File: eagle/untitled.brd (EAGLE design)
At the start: 50 x 50 mm, 58 parts, among them J1 JTAG, Q1 16MHz, U1 MMA3202KEG

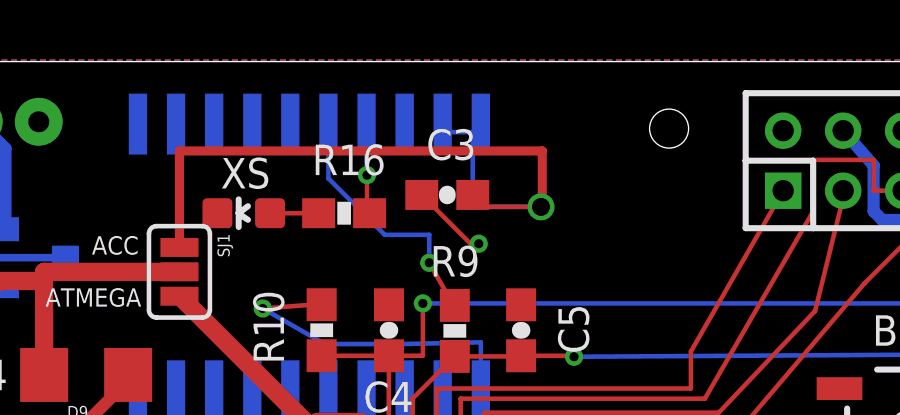
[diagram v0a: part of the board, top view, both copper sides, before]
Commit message: Add self test pad for accelerometer.
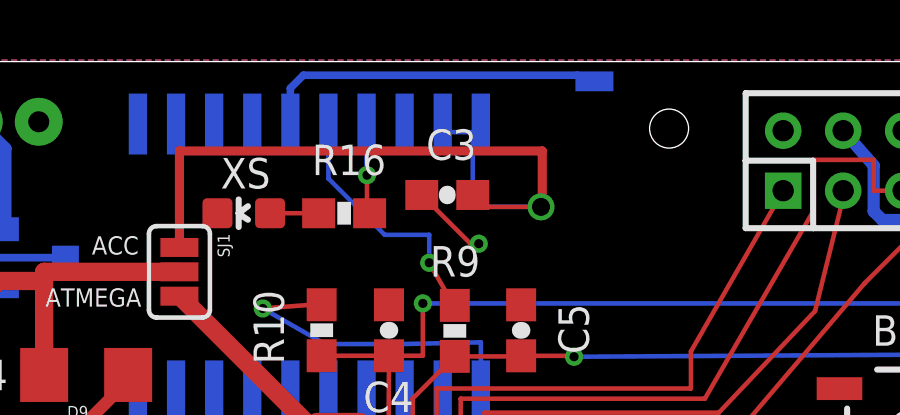
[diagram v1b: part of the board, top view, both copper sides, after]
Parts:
- added TP1: TESTPAD, gipi:TP_SEMICIRCULAR
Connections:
- new net N$28: TP1.P$2, U1.P$5
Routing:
- net N$28: track 0.00 -> 11.6 mm
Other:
- board text added: "S-TEST"
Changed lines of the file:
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@@
 <setting verticaltext="up"/>
 </settings>
-<grid distance="100" unitdist="mil" unit="mil" style="lines" multiple="1" display="yes" altdistance="10" altunitdist="mil" altunit="mil"/>
+<grid distance="100" unitdist="mil" unit="mil" style="lines" multiple="1" display="yes" altdistance="1" altunitdist="mil" altunit="mil"/>
 <layers>
 <layer number="1" name="Top" color="4" fill="1" visible="yes" active="yes"/>
@@
 <hole x="30.48" y="33.02" drill="1.3"/>
 <hole x="35.56" y="76.2" drill="1.3"/>
+<text x="34.3662" y="76.454" size="0.6096" layer="22" font="vector" ratio="16" rot="SMR0">S-TEST</text>
 </plain>
 <attributes>
@@
 <attribute name="VALUE" x="11.26345" y="69.99168125" size="1.27" layer="28" rot="MR90"/>
 </element>
+<element name="TP1" library="gipi" package="TP_SEMICIRCULAR" value="TESTPAD" x="33.0708" y="77.7748" rot="MR0"/>
 </elements>
 <signals>
@@
 <wire x1="13.43845" y1="75.5376375" x2="13.43845" y2="72.84668125" width="0.4064" layer="16"/>
 </signal>
+<signal name="N$28">
+<contactref element="U1" pad="P$5"/>
+<wire x1="22.935309375" y1="76.349809375" x2="22.935309375" y2="77.545309375" width="0.254" layer="16"/>
+<wire x1="22.935309375" y1="77.545309375" x2="23.368" y2="77.978" width="0.254" layer="16"/>
+<wire x1="23.368" y1="77.978" x2="32.512" y2="77.978" width="0.254" layer="16"/>
+<contactref element="TP1" pad="P$2"/>
+<wire x1="32.512" y1="77.978" x2="32.639" y2="77.851" width="0.254" layer="16"/>
+<wire x1="32.639" y1="77.851" x2="33.0708" y2="77.7748" width="0.254" layer="16"/>
+</signal>
 </signals>

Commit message: 2nd version in production.
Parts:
- BOOST: value V_REG_TPS61040SMD -> TPS61040
- D13: value DIODE -> MBRA140; device gipi:1206 -> SparkFun-DiscreteSemi:SMA-DIODE
- L1: value (none) -> 3.3uH; device SparkFun-Passives:0603 -> SparkFun-Passives:1210
- N-FET: value P-CHANNEL-MOSFET -> N-CHANNEL-MOSFET-BSS138
- RA: value 1k -> 3.09k
- moved L1 0.80 mm to (8.53, 71.9)
- renumbered R17 to RA, R18 to RB
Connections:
- net N$39: now also D13.A; no longer D13.P$1
- net VBATT: now also D13.C; no longer D13.P$2
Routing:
- net N$38: track 10.2 -> 11.0 mm
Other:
- board text added: "V2"

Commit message: Fix mess with ground.
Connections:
- removed net GN: C4.1, C5.1, C6.2, D1.C, D2.C, D3.C, D4.C, D5.C, D6.C, D7.C, D8.C, D9.C, J1.10, J1.2, JP1.12, JP5.6, S1.1, S1.2, S2.3, XS.C
- removed net GND-ISO: BOOST.2, C1.1, C2.1, C3.1, C7.1, C9.1, JP2.GND, JP6.2, N-FET.1, RB.1, U$1.15, U$1.23, U$1.35, U$1.43, U$1.5, U1.P$20, U1.P$8
- new net GND: BOOST.2, C1.1, C2.1, C3.1, C4.1, C5.1, C6.2, C7.1, C9.1, D1.C, D2.C, D3.C, D4.C, D5.C, D6.C, D7.C, D8.C, D9.C, J1.10, J1.2, JP1.12, JP2.GND, JP5.6, JP6.2, N-FET.1, RB.1, S1.1, S1.2, S2.3, U$1.15, U$1.23, U$1.35, U$1.43, U$1.5, U1.P$20, U1.P$8, XS.C
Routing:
- net GND-ISO: track 27.2 -> 0.00 mm, vias 6 -> 0
- net GN: track 5.72 -> 0.01 mm
- added copper zone on layer 1, net GND
- added copper zone on layer 16, net GND
- removed copper zone on layer 1, net GN
- removed copper zone on layer 16, net GND-ISO
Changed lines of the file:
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@@
 </signal>
 <signal name="GN">
-<contactref element="S1" pad="2"/>
-<contactref element="S1" pad="1"/>
-<contactref element="C5" pad="1"/>
-<contactref element="C4" pad="1"/>
-<contactref element="C6" pad="2"/>
-<contactref element="JP5" pad="6"/>
-<contactref element="D1" pad="C"/>
-<contactref element="D2" pad="C"/>
-<contactref element="D3" pad="C"/>
-<contactref element="D4" pad="C"/>
-<contactref element="D5" pad="C"/>
-<contactref element="D6" pad="C"/>
-<contactref element="D7" pad="C"/>
-<contactref element="D8" pad="C"/>
-<wire x1="2.4892" y1="30.0228" x2="2.413" y2="29.996" width="0.1524" layer="1"/>
-<wire x1="8.7376" y1="30.0228" x2="8.763" y2="29.996" width="0.1524" layer="1"/>
-<contactref element="J1" pad="2"/>
-<contactref element="J1" pad="10"/>
 <wire x1="27.6352" y1="30.48" x2="27.649396875" y2="30.48" width="0.1524" layer="1"/>
-<wire x1="7.703009375" y1="77.216" x2="2.115009375" y2="77.216" width="0.1524" layer="1"/>
-<contactref element="D9" pad="C"/>
-<contactref element="S2" pad="3"/>
-<contactref element="XS" pad="C"/>
-<contactref element="JP1" pad="12"/>
-<polygon width="0.3048" layer="1">
-<vertex x="0.508" y="78.486"/>
-<vertex x="50.673" y="78.486"/>
-<vertex x="50.673" y="28.321"/>
-<vertex x="0.508" y="28.321"/>
-</polygon>
 </signal>
 <signal name="N$19">
@@
 <wire x1="6.4764125" y1="71.7287" x2="6.4264125" y2="68.509334375" width="0.3048" layer="16"/>
 </signal>
-<signal name="GND-ISO">
-<contactref element="C7" pad="1"/>
-<contactref element="BOOST" pad="2"/>
-<contactref element="RB" pad="1"/>
-<contactref element="C9" pad="1"/>
-<polygon width="0.1524" layer="16">
-<vertex x="0.508" y="78.486"/>
-<vertex x="50.673" y="78.486"/>
-<vertex x="50.673" y="28.321"/>
-<vertex x="0.508" y="28.321"/>
-</polygon>
-<contactref element="U1" pad="P$20"/>
-<contactref element="U1" pad="P$8"/>
-<contactref element="C3" pad="1"/>
-<contactref element="U$1" pad="35"/>
-<contactref element="JP2" pad="GND"/>
-<contactref element="U$1" pad="43"/>
-<contactref element="U$1" pad="5"/>
-<contactref element="C2" pad="1"/>
-<contactref element="U$1" pad="15"/>
-<contactref element="U$1" pad="23"/>
-<contactref element="C1" pad="1"/>
-<via x="29.893209375" y="61.946359375" extent="1-16" drill="0.3048" diameter="0.3048"/>
-<via x="24.177065625" y="62.79319375" extent="1-16" drill="0.3048" diameter="0.03048125"/>
-<wire x1="24.613" y1="64.601" x2="24.613" y2="62.79319375" width="0.508" layer="1"/>
-<wire x1="24.613" y1="62.79319375" x2="24.177065625" y2="62.79319375" width="0.508" layer="1"/>
-<via x="23.880675" y="59.913953125" extent="1-16" drill="0.3048" diameter="0.03048125"/>
-<wire x1="22.013" y1="59.601" x2="23.567721875" y2="59.601" width="0.508" layer="1"/>
-<wire x1="23.567721875" y1="59.601" x2="23.880675" y2="59.913953125" width="0.508" layer="1" curve="90"/>
-<via x="29.00403125" y="54.875278125" extent="1-16" drill="0.6" diameter="0.03048125"/>
-<wire x1="26.213" y1="53.001" x2="26.213" y2="54.875278125" width="0.508" layer="1"/>
-<wire x1="26.213" y1="54.875278125" x2="29.00403125" y2="54.875278125" width="0.508" layer="1"/>
-<wire x1="29.00403125" y1="54.875278125" x2="29.00403125" y2="54.801" width="0.1524" layer="1"/>
-<wire x1="29.00403125" y1="54.801" x2="33.613" y2="54.801" width="0.508" layer="1"/>
-<via x="24.177065625" y="42.34210625" extent="1-16" drill="0.3048" diameter="0.3048"/>
-<wire x1="20.408" y1="42.291" x2="24.125959375" y2="42.291" width="0.1524" layer="1"/>
-<wire x1="24.125959375" y1="42.291" x2="24.177065625" y2="42.34210625" width="0.1524" layer="1"/>
-<via x="29.215740625" y="72.362440625" extent="1-16" drill="0.3048" diameter="0.3048"/>
-<wire x1="27.598" y1="42.291" x2="24.228171875" y2="42.291" width="0.1524" layer="1"/>
-<wire x1="24.228171875" y1="42.291" x2="24.177065625" y2="42.34210625" width="0.1524" layer="1"/>
-<contactref element="JP6" pad="2"/>
-<wire x1="27.3163375" y1="73.987053125" x2="28.94095" y2="72.362440625" width="0.1524" layer="1"/>
-<wire x1="28.94095" y1="72.362440625" x2="29.215740625" y2="72.362440625" width="0.1524" layer="1"/>
-<contactref element="N-FET" pad="1"/>
-<wire x1="31.013" y1="64.601" x2="31.013" y2="61.946359375" width="0.508" layer="1"/>
-<wire x1="31.013" y1="61.946359375" x2="29.893209375" y2="61.946359375" width="0.508" layer="1"/>
-</signal>
 <signal name="N$41">
 <contactref element="BOOST" pad="3"/>
@@
 <wire x1="32.639" y1="77.851" x2="33.0708" y2="77.7748" width="0.254" layer="16"/>
 </signal>
+<signal name="GND">
+<contactref element="JP2" pad="GND"/>
+<contactref element="U$1" pad="23"/>
+<contactref element="C2" pad="1"/>
+<contactref element="U$1" pad="35"/>
+<contactref element="U$1" pad="5"/>
+<contactref element="U$1" pad="15"/>
+<contactref element="U$1" pad="43"/>
+<contactref element="C1" pad="1"/>
+<contactref element="S1" pad="2"/>
+<contactref element="S1" pad="1"/>
+<contactref element="D9" pad="C"/>
+<contactref element="J1" pad="2"/>
+<contactref element="J1" pad="10"/>
+<contactref element="JP5" pad="6"/>
+<contactref element="D1" pad="C"/>
+<contactref element="D2" pad="C"/>
+<contactref element="D4" pad="C"/>
+<contactref element="D3" pad="C"/>
+<contactref element="D8" pad="C"/>
+<contactref element="D5" pad="C"/>
+<contactref element="JP1" pad="12"/>
+<contactref element="D7" pad="C"/>
+<contactref element="D6" pad="C"/>
+<contactref element="S2" pad="3"/>
+<contactref element="C5" pad="1"/>
+<contactref element="C4" pad="1"/>
+<contactref element="XS" pad="C"/>
+<contactref element="U1" pad="P$20"/>
+<contactref element="U1" pad="P$8"/>
+<contactref element="C3" pad="1"/>
+<contactref element="C9" pad="1"/>
+<contactref element="N-FET" pad="1"/>
+<contactref element="BOOST" pad="2"/>
+<contactref element="C7" pad="1"/>
+<contactref element="RB" pad="1"/>
+<contactref element="JP6" pad="2"/>
+<polygon width="0.1524" layer="16">
+<vertex x="0.508" y="78.486"/>
+<vertex x="50.673" y="78.486"/>
+<vertex x="50.673" y="28.321"/>
+<vertex x="0.508" y="28.321"/>
+</polygon>
+<polygon width="0.3048" layer="1">
+<vertex x="0.508" y="78.486"/>
+<vertex x="50.673" y="78.486"/>
+<vertex x="50.673" y="28.321"/>
+<vertex x="0.508" y="28.321"/>
+</polygon>
+<contactref element="C6" pad="2"/>
+<via x="29.5656" y="62.3062" extent="1-16" drill="0.6" shape="octagon"/>
+</signal>
 </signals>

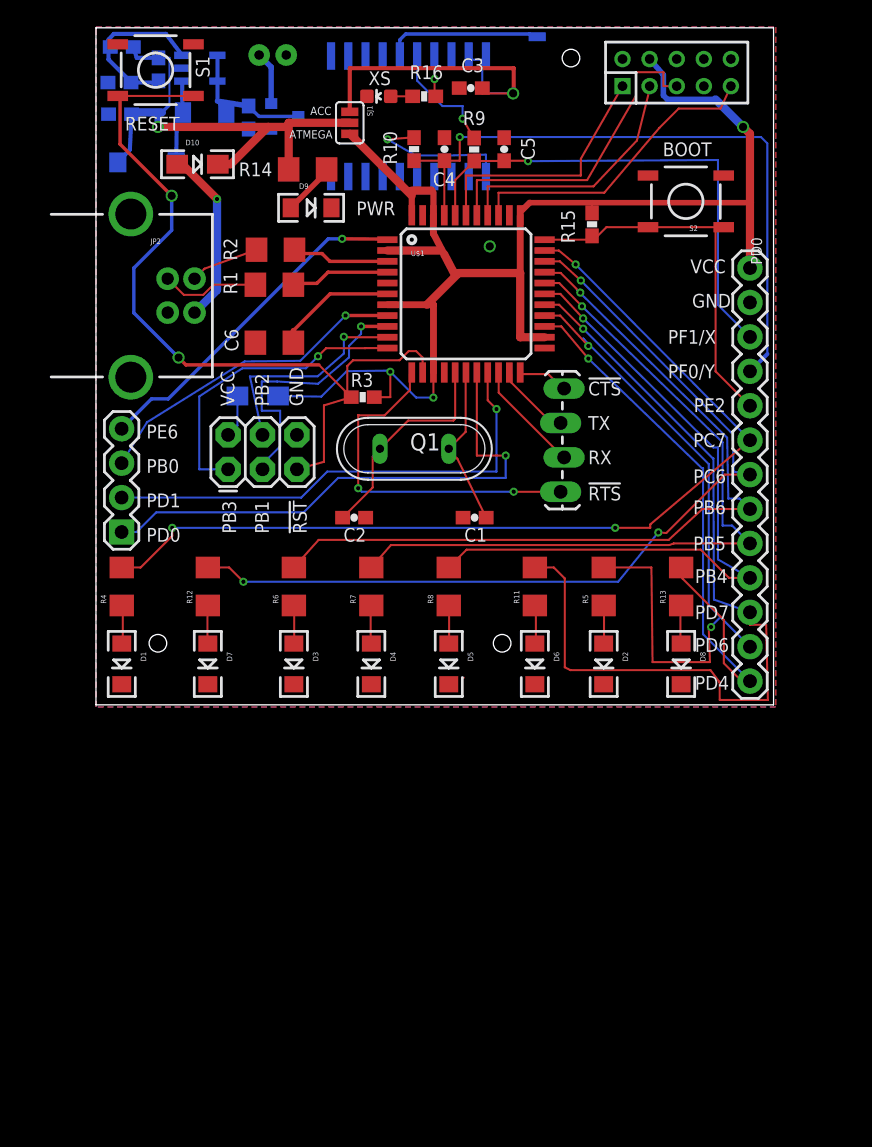
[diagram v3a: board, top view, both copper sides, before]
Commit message: Update ciaoduino's eagle files.
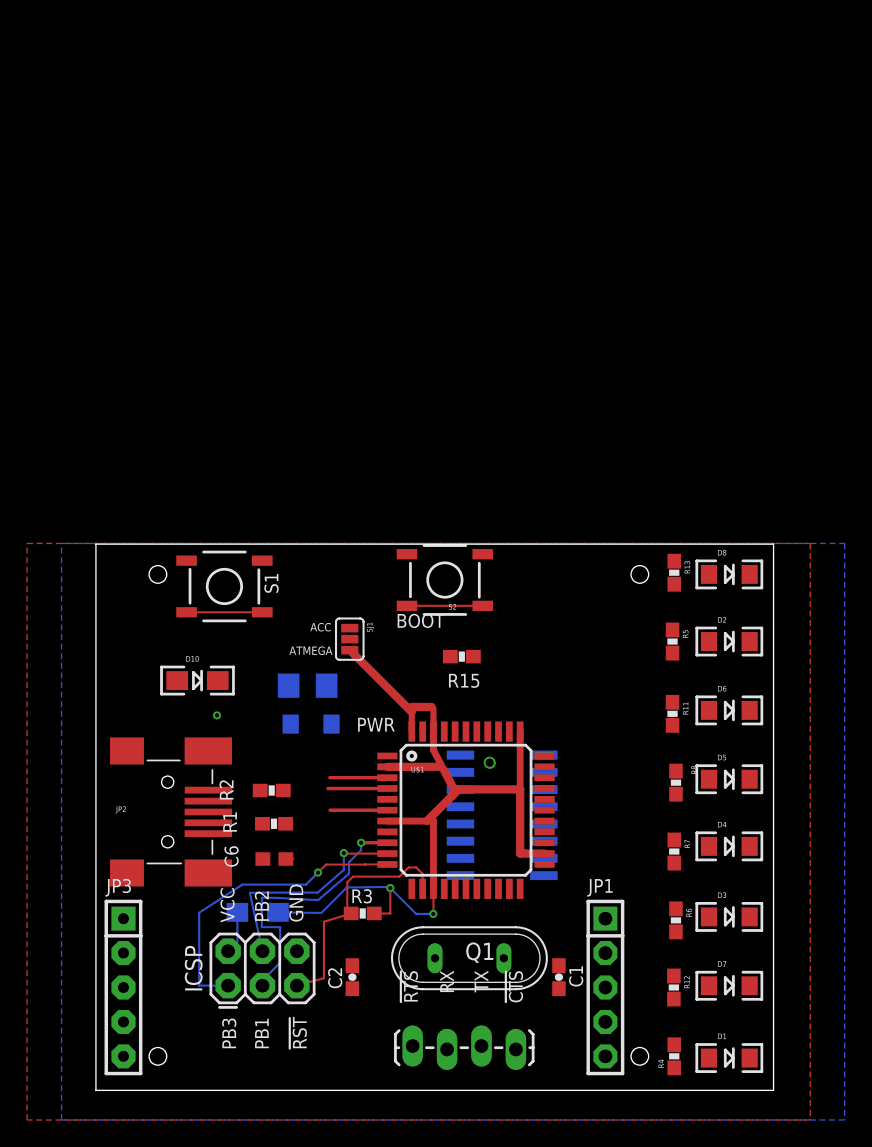
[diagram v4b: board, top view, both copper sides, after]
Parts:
- removed BOOST: TPS61040, SparkFun-PowerIC:SOT23-5
- removed C3: 0.1uF, SparkFun-Capacitors:0603-CAP
- removed C4, C5, C7, C8, C9: 10nF, SparkFun-Capacitors:0603-CAP
- removed D13: MBRA140, SparkFun-DiscreteSemi:SMA-DIODE
- removed J1: JTAG, con-headers-jp:DIL-2MM-2X05
- removed JP6: M02JST-PTH-VERT, SparkFun-Connectors:JST-2-PTH-VERT
- removed L1: 3.3uH, SparkFun-Passives:1210
- removed N-FET: N-CHANNEL-MOSFET-BSS138, GeekAmmo:SOT23-3
- removed R10, R16, R9, RB: 1k, SparkFun-Passives:0603-RES
- removed RA: 3.09k, SparkFun-Passives:0603-RES
- removed TP1: TESTPAD, gipi:TP_SEMICIRCULAR
- removed U$2: KITTEN, gipi:KITTEN
- removed U1: MMA3202KEG, gipi:SOIC20
- removed XS: (no value), SparkFun-LED:LED-0603
- added IC1: 74LS595D, 74xx-us:SO16
- C6: device eagle-ltspice:C1206 -> eagle-ltspice:C0603
- JP1: value M13 -> F-1X05-SIP-100-40; device SparkFun-Connectors:1X13 -> con-headers-jp:SIP-100-05-40
- JP2: value USB-B -> USBOLD; device SparkFun-Connectors:USB-B-PTH -> SparkFun-Connectors:USB-MINIB-OLD
- JP3: value (none) -> F-1X05-SIP-100-32; device SparkFun-Connectors:1X04 -> con-headers-jp:SIP-100-05-32
- R1, R2: device SparkFun-Passives:1206 -> SparkFun-Passives:0603-RES
- R11, R12, R13, R4, R5, R6, R7, R8: value (none) -> 1k; device SparkFun-Passives:1206 -> SparkFun-Passives:0603-RES
- moved R4 53.5 mm to (43.2, 2.54)
- moved D1 53.4 mm to (47.2, 2.41), turned to 0 degrees
- moved R12 45.4 mm to (43.2, 7.62), turned to 270 degrees
- moved D7 45.2 mm to (47.2, 7.75), turned to 0 degrees
- moved JP4 42.3 mm to (23.9, 3.30), turned to 0 degrees
- moved R2 39.9 mm to (13.5, 22.2)
- moved R1 39.8 mm to (13.6, 19.7)
- moved S1 38.4 mm to (9.99, 37.2)
- moved R14 38.1 mm to (16.1, 29.9), flipped to the bottom
- moved C6 38.1 mm to (13.7, 17.1)
- moved D12 38.1 mm to (12.4, 13.2)
- moved JP2 38.1 mm to (5.80, 20.6)
- moved JP5 38.1 mm to (10.3, 7.76)
- moved U$1 38.1 mm to (27.8, 20.7)
- moved D10 38.1 mm to (8.00, 30.3)
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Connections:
- removed net N$36: R16.2, XS.A
- removed net N$38: BOOST.4, BOOST.5, C7.2, L1.1, N-FET.3
- removed net N$39: BOOST.1, D13.A, L1.2
- removed net N$41: BOOST.3, C8.1, RA.1, RB.2
- removed net X: C5.2, JP1.11, R9.2, U$1.40
- removed net Y: C4.2, JP1.10, R10.2, U$1.41
- new net RCLK: IC1.12, JP1.2
- new net SCLK: IC1.11, JP1.3
- new net SER: IC1.14, JP1.1
- new net VCC: IC1.16
- net GND: now also IC1.13, IC1.8, JP1.4, S2.4; no longer BOOST.2, C3.1, C4.1, C5.1, C7.1, C9.1, J1.10, J1.2, JP1.12, JP6.2, N-FET.1, RB.1, U1.P$20, U1.P$8, XS.C
- net N$1: now also IC1.15, R13.2; no longer R9.1, U1.P$100
- net N$21: now also IC1.1, R12.2; no longer R10.1, U1.P$11
- net N$22: now also IC1.2, R11.2; no longer J1.1, U$1.39
- net N$25: now also IC1.3, R8.2; no longer J1.5, U$1.38
- net N$26: now also IC1.4, R7.2; no longer J1.3, U$1.37
- net N$27: now also IC1.5, R6.2; no longer J1.9, U$1.36
- net N$28: now also IC1.6, R5.2; no longer TP1.P$2, U1.P$5
- net N$33: now also IC1.7, R4.2; no longer JP6.1, N-FET.2
- net N$35: now also JP1.5; no longer R16.1, U1.P$7
- net PB0: no longer JP3.3
- net PB4: no longer JP1.4, R8.2
- net PB5: no longer JP1.5, R7.2
- net PB6: no longer JP1.6, R6.2
- net PC6: no longer JP1.7, R12.2
- net PC7: no longer JP1.8, R4.2
- net PD0: no longer JP3.1
- net PD1: no longer JP3.2
- net PD4: no longer JP1.1, R13.2
- net PD6: no longer JP1.2, R5.2
- net PD7: no longer JP1.3, R11.2
- net PE2: no longer JP1.9
- net PE6: no longer JP3.4
- net VBATT: no longer C8.2, C9.2, D13.C, RA.2
- net VCC1: no longer J1.4, JP1.13
- net VCC2: no longer C3.2, U1.P$10, U1.P$9
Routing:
- net PC7: track 71.4 -> 0.00 mm, vias 3 -> 0
- net PC6: track 67.1 -> 0.00 mm, vias 3 -> 0
- net PD7: track 63.9 -> 0.00 mm, vias 1 -> 0
- net PB6: track 61.0 -> 0.00 mm, vias 1 -> 0
- net PB5: track 55.3 -> 0.00 mm, vias 1 -> 0
- net PB4: track 52.1 -> 0.00 mm, vias 1 -> 0
- net PD6: track 51.1 -> 0.00 mm, vias 2 -> 0
- net Y: track 49.4 -> 0.00 mm, vias 1 -> 0
- net PD4: track 44.0 -> 0.00 mm, vias 1 -> 0
- net PD0: track 39.9 -> 0.00 mm, vias 1 -> 0
- net VCC1: track 107.7 -> 69.0 mm, vias 3 -> 2
- net VBATT: track 37.5 -> 0.00 mm, vias 1 -> 0
- net N$17: track 61.1 -> 23.7 mm, vias 2 -> 0
- net X: track 36.6 -> 0.00 mm, vias 1 -> 0
- net PD1: track 36.0 -> 0.00 mm, vias 1 -> 0
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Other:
- board size 50 x 50 mm -> 50 x 40.3 mm
- board text added: "V3"
- board text removed: "PB0"
- board text removed: "PB4"
- board text removed: "PB5"
- board text removed: "PB6"
- board text removed: "PC6"
- board text removed: "PC7"
- board text removed: "PD0"
- board text removed: "PD1"
- board text removed: "PD4"
- board text removed: "PD6"
- board text removed: "PD7"
- board text removed: "PE2"
- board text removed: "PE6"
- board text removed: "PF0/Y"
- board text removed: "PF1/X"
- board text removed: "RESET"
- board text removed: "S-TEST"
- board text removed: "V2"
